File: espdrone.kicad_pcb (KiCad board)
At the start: 6 copper layers, 60 x 60 mm, 504 parts, among them J10 Conn_01x04, J11 Conn_01x04, J12 Conn_01x04, J4 Conn_01x06, J5 Conn_Coaxial, J6 Conn_01x06, J7 Conn_01x06, J8 Conn_01x04, J9 Conn_01x04, Q1 NMOS, Q10 NMOS, Q11 NMOS, Q12 NMOS, Q13 NMOS, Q14 NMOS, Q15 NMOS, Q16 NMOS, Q17 NMOS, Q18 NMOS, Q19 NMOS, Q2 NMOS, Q20 NMOS, Q21 NMOS, Q22 NMOS, Q23 NMOS, Q24 NMOS, Q25 NMOS, Q26 NMOS, Q27 NMOS, Q28 NMOS, Q3 NMOS, Q4 NMOS, Q5 NMOS, Q6 NMOS, Q7 NMOS, Q8 NMOS, Q9 NMOS, U10 FPC-1.0FX-15PWCR-H20, U11 VL53L1CXV0FY1, U12 LIS2MDL, U13 LSM6DS3, U14 PMW3901MB-TXQT_C43496881, U15 STM32G071K8U6, U16 DRV8328ARUYR, U17 INA180A2, U18 STM32G071K8U6, U19 DRV8328ARUYR, U2 USBLC6-2P6, U20 INA180A2, U21 STM32G071K8U6, U22 DRV8328ARUYR, U23 INA180A2, U24 STM32G071K8U6, U25 DRV8328ARUYR, U26 INA180A2, U3 W25Q128JVP, U4 ESP32-C5HF4, U5 LFD182G45DCHD277, U6 TLV62569DBV, U7 XC6206P182MR_C347373, U8 TPS63070RNMR, U9 TPS2121RUXR, Y1 Crystal_GND24, Y2 Crystal_GND24

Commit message: Do local layout of power sheet
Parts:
- moved C59 55.1 mm to (281.2, 112.9)
- moved C61 54.2 mm to (281.2, 114.7)
- moved C65 54.2 mm to (281.2, 116.7)
- moved R38 43.2 mm to (264.2, 87.0), turned to 90 degrees
- moved R29 41.1 mm to (260.2, 91.0)
- moved R37 41.0 mm to (264.2, 89.0), turned to 90 degrees
- moved R30 40.7 mm to (258.2, 91.0)
- moved L3 39.9 mm to (264.5, 96.4), turned to -90 degrees
- moved R31 39.0 mm to (260.0, 98.6)
- moved C74 38.4 mm to (277.6, 97.1), turned to 180 degrees
- moved TP2 37.9 mm to (280.4, 103.8)
- moved TP1 37.9 mm to (275.4, 103.8)
- moved R36 37.6 mm to (261.2, 88.5), turned to 90 degrees
- moved C73 34.3 mm to (257.5, 108.0), turned to -90 degrees
- moved R33 34.0 mm to (260.2, 88.5), turned to 90 degrees
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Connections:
- R31 pad 1: Net-(R31-Pad1) -> FB_DCDC
- R32 pad 2: Net-(R31-Pad1) -> FB_DCDC

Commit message: Get rid of 1.8V LDO and use P4 VDDO4 instead
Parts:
- removed C59, C65: 1u, Capacitor_SMD:C_0402_1005Metric
- removed C61: 100n, Capacitor_SMD:C_0402_1005Metric
- removed U7: XC6206P182MR_C347373, easyeda2kicad:SOT-23-3_L3.0-W1.7-P0.95-LS2.9-BR
- moved C74 5.84 mm to (273.6, 92.9)
- moved TP1 5.84 mm to (271.4, 99.5)
- moved TP2 5.84 mm to (276.4, 99.5)
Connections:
- C33 pad 1: /MCU/VDDO_4 -> VDDO_4
- C88 pad 2: +1V8 -> VDDO_4
- C90 pad 2: +1V8 -> VDDO_4
- C92 pad 2: +1V8 -> VDDO_4
- U1 pad 74: /MCU/VDDO_4 -> VDDO_4
- U14 pad 2: +1V8 -> VDDO_4

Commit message: Do some ESC layouting
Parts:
- removed U17: INA180A2, Package_TO_SOT_SMD:SOT-23-5
- added U27: INA190A3IDCKR, easyeda2kicad:SC-70-6_L2.0-W1.3-P0.65-LS2.1-BL, F.Cu at (197.4, 70.5)
- added U28: INA190A3IDCKR, easyeda2kicad:SC-70-6_L2.0-W1.3-P0.65-LS2.1-BL, F.Cu at (197.4, 76.6)
- added U29: INA190A3IDCKR, easyeda2kicad:SC-70-6_L2.0-W1.3-P0.65-LS2.1-BL, F.Cu at (202.6, 70.5)
- added U7: INA190A3IDCKR, easyeda2kicad:SC-70-6_L2.0-W1.3-P0.65-LS2.1-BL, B.Cu at (127.2, 86.8)
- C102, C103, C105, C107, C109, C110, C111, C117, C119, R62, R63, R65, R66, R71, R72, R77, R80, R85, U16: moved to B.Cu
- TP11, TP12, TP13, TP14, TP15, TP16, TP17, TP18, TP19, TP23, TP24, TP25, TP26, TP27, TP28, TP29, TP30, TP31, TP35, TP36, TP37, TP38, TP39, TP40, TP41, TP42, TP43, TP47, TP48, TP49, TP50, TP51, TP52, TP53, TP54, TP55: footprint TestPoint:TestPoint_Pad_D1.0mm -> easyeda2kicad:TestPoint_Pad_D1.0mm_No_Courtyard
- U20, U23, U26: footprint Package_TO_SOT_SMD:SOT-23-5 -> Package_TO_SOT_SMD:SOT-363_SC-70-6
- moved C73 168.7 mm to (103.2, 176.0)
- moved R34 168.7 mm to (107.2, 174.0)
- moved R35 168.7 mm to (107.2, 176.0)
- moved R39 168.7 mm to (103.2, 174.0)
- moved U9 168.7 mm to (105.2, 175.0)
- moved C60 168.4 mm to (104.8, 161.2)
- moved R29 168.4 mm to (106.8, 160.2)
- moved R30 168.4 mm to (104.8, 160.2)
- moved C64 167.6 mm to (106.8, 156.4)
- moved C70 167.6 mm to (114.1, 154.8)
- moved C71 167.6 mm to (114.1, 152.8)
- moved U8 167.6 mm to (110.2, 157.2)
- moved C62 167.6 mm to (106.0, 152.5)
- moved C63 167.6 mm to (106.0, 154.5)
- moved C68 167.6 mm to (111.1, 159.2)
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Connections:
- Q10 pad 1: Net-(Q10-D) -> /Motors/ESC1/PHASE_C
- Q11 pad 3: Net-(Q11-S) -> /Motors/ESC2/PHASE_A
- Q12 pad 1: Net-(Q11-S) -> /Motors/ESC2/PHASE_A
- Q13 pad 3: Net-(Q13-S) -> /Motors/ESC2/PHASE_B
- Q14 pad 1: Net-(Q13-S) -> /Motors/ESC2/PHASE_B
- Q15 pad 3: Net-(Q15-S) -> /Motors/ESC2/PHASE_C
- Q16 pad 1: Net-(Q15-S) -> /Motors/ESC2/PHASE_C
- Q17 pad 3: Net-(Q17-S) -> /Motors/ESC3/PHASE_A
- Q18 pad 1: Net-(Q17-S) -> /Motors/ESC3/PHASE_A
- Q19 pad 3: Net-(Q19-S) -> /Motors/ESC3/PHASE_B
- Q20 pad 1: Net-(Q19-S) -> /Motors/ESC3/PHASE_B
- Q21 pad 3: Net-(Q21-S) -> /Motors/ESC3/PHASE_C
- Q22 pad 1: Net-(Q21-S) -> /Motors/ESC3/PHASE_C
- Q23 pad 3: Net-(Q23-S) -> /Motors/ESC4/PHASE_A
- Q24 pad 1: Net-(Q23-S) -> /Motors/ESC4/PHASE_A
- Q25 pad 3: Net-(Q25-S) -> /Motors/ESC4/PHASE_B
- Q26 pad 1: Net-(Q25-S) -> /Motors/ESC4/PHASE_B
- Q27 pad 3: Net-(Q27-S) -> /Motors/ESC4/PHASE_C
- Q28 pad 1: Net-(Q27-S) -> /Motors/ESC4/PHASE_C
- Q5 pad 3: Net-(Q5-S) -> /Motors/ESC1/PHASE_A
- Q6 pad 1: Net-(Q5-S) -> /Motors/ESC1/PHASE_A
- Q7 pad 3: Net-(Q7-S) -> /Motors/ESC1/PHASE_B
- Q8 pad 1: Net-(Q7-S) -> /Motors/ESC1/PHASE_B
- Q9 pad 3: Net-(Q10-D) -> /Motors/ESC1/PHASE_C
- R122 pad 2: Net-(R122-Pad2) -> Net-(U28-OUT)
- R147 pad 2: Net-(R147-Pad2) -> Net-(U29-OUT)
- R97 pad 2: Net-(R97-Pad2) -> Net-(U27-OUT)

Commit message: Progress on bridge layout
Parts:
- C109, C110, C111, R77, R80, R85: moved to F.Cu
- R69, R70, R73, R74, R81, R82: moved to B.Cu
- moved Q10 18.0 mm to (129.5, 61.9)
- moved Q9 18.0 mm to (129.8, 65.8)
- moved TP22 18.0 mm to (126.5, 58.6)
- moved Q7 17.6 mm to (124.8, 65.8)
- moved Q8 17.6 mm to (124.4, 61.9)
- moved TP21 17.6 mm to (127.8, 58.5)
- moved R71 17.5 mm to (124.8, 65.8)
- moved C117 17.5 mm to (127.1, 70.2)
- moved C119 17.5 mm to (127.6, 68.7)
- moved R72 17.5 mm to (126.6, 68.7)
- moved U7 17.5 mm to (125.1, 69.4)
- moved Q5 17.3 mm to (119.8, 65.8)
- moved TP20 17.3 mm to (122.9, 58.5)
- moved Q6 17.3 mm to (119.5, 61.9)
- moved C110 16.8 mm to (125.5, 70.0), turned to 180 degrees
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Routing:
- net /Motors/ESC1/LSS: track 0.00 -> 17.9 mm, vias 0 -> 3
- net /Motors/ESC1/PHASE_C: track 0.00 -> 15.4 mm
- net /Motors/ESC1/PHASE_B: track 0.00 -> 14.9 mm
- net /Motors/ESC1/PHASE_A: track 0.00 -> 14.8 mm
- net Net-(Q10-G): track 0.00 -> 11.7 mm, vias 0 -> 1
- net GND: track 0.00 -> 11.6 mm
- net Net-(Q9-G): track 0.00 -> 9.36 mm, vias 0 -> 1
- net /Motors/ESC1/ISENSE: track 0.00 -> 1.01 mm
- net Net-(U7-OUT): track 0.00 -> 0.92 mm
- net +BATT: track 0.00 -> 0.11 mm, vias 0 -> 36

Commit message: Okayish bridge layout
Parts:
- moved R85 8.26 mm to (123.2, 75.2), turned to -90 degrees
- moved R82 6.14 mm to (126.1, 73.5), turned to 180 degrees
- moved R80 5.66 mm to (122.0, 75.2), turned to -90 degrees
- moved C111 5.10 mm to (125.7, 72.4)
- moved C110 4.15 mm to (122.2, 72.4)
- moved R81 4.01 mm to (126.1, 72.0), turned to 180 degrees
- moved R77 3.81 mm to (120.8, 75.2), turned to -90 degrees
- moved C109 3.32 mm to (118.5, 72.4)
- moved C105 2.14 mm to (116.5, 77.8), turned to -90 degrees
- moved C107 1.63 mm to (118.4, 78.3)
- moved TP22 0.78 mm to (127.2, 58.6)
- moved Q5 0.36 mm to (119.4, 65.8)
- moved Q6 0.36 mm to (119.1, 61.9)
- moved TP20 0.36 mm to (122.6, 58.5)
- moved Q10 0.28 mm to (129.8, 61.9)
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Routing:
- net /Motors/ESC1/GLA: track 0.00 -> 12.5 mm
- net /Motors/ESC1/GHA: track 0.00 -> 7.53 mm
- net Net-(Q7-G): track 0.32 -> 7.20 mm, vias 0 -> 1
- net Net-(Q8-G): track 0.00 -> 6.35 mm, vias 0 -> 1
- net GND: track 11.6 -> 17.9 mm, vias 0 -> 12
- net Net-(Q10-G): track 11.7 -> 17.8 mm
- net Net-(U16-VDSLVL): track 0.00 -> 5.92 mm
- net /Motors/ESC1/GHB: track 0.00 -> 5.52 mm
- net /Motors/ESC1/BSTA: track 0.00 -> 5.22 mm, vias 0 -> 1
- net /Motors/ESC1/GLB: track 0.00 -> 5.11 mm
- net +BATT: track 0.11 -> 5.09 mm
- net Net-(U16-DT): track 0.00 -> 4.37 mm
- net /Motors/ESC1/GHC: track 0.00 -> 4.19 mm
- net Net-(Q9-G): track 9.36 -> 13.5 mm
- net Net-(U16-BSTC): track 0.00 -> 3.69 mm, vias 0 -> 1
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- added copper zone on F.Cu, net */LSS
- added copper zone on B.Cu, net /Motors/ESC1/LSS
- added copper zone on F.Cu, net /Motors/ESC1/LSS
- added copper zone on F.Cu, net /Motors/ESC1/PHASE_A

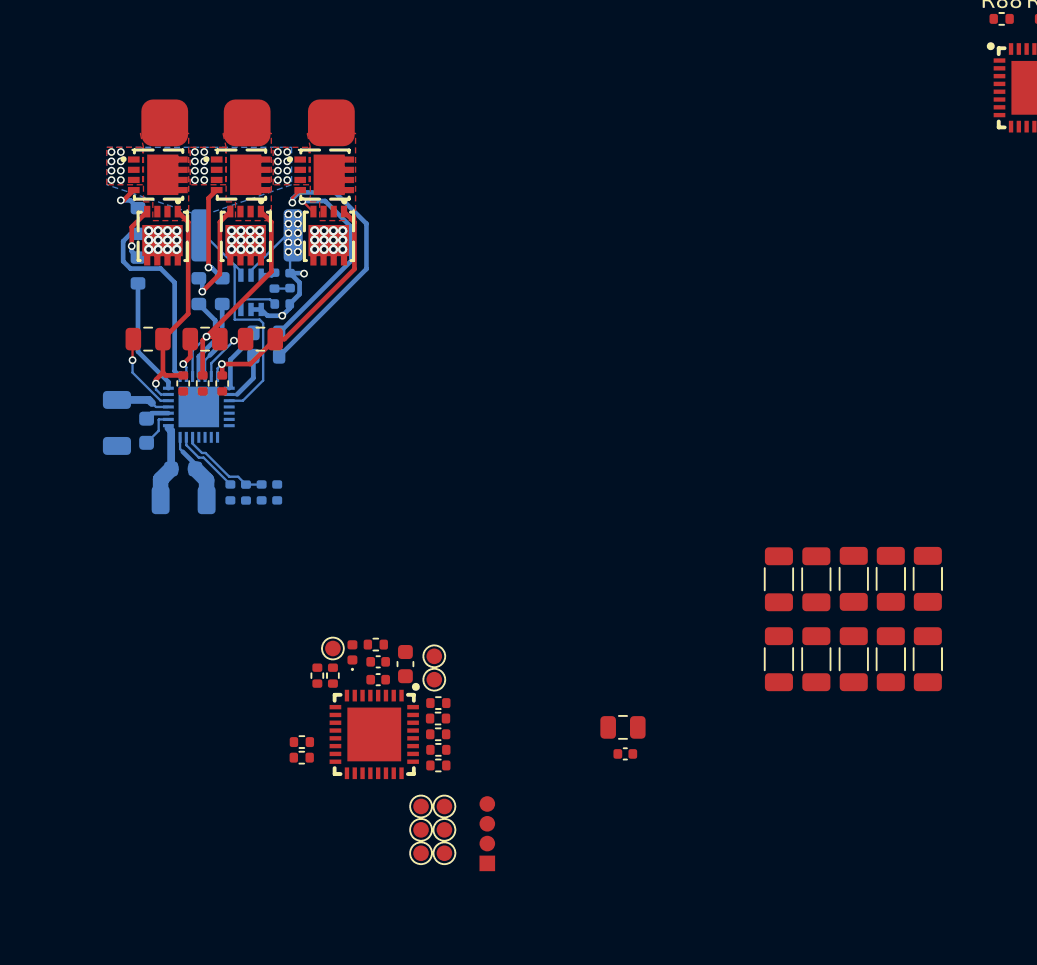
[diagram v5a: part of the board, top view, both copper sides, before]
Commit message: ESC mostly done apart from STM routing
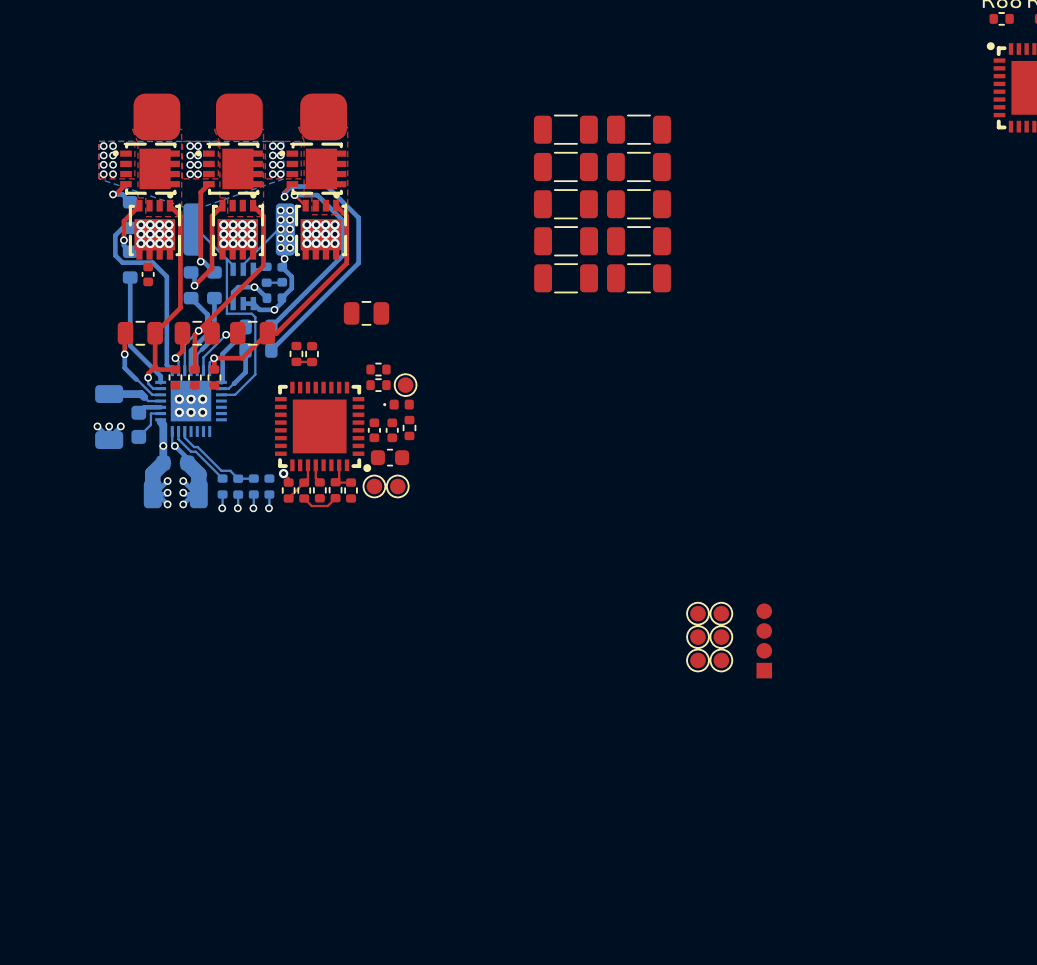
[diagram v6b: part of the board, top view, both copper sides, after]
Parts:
- moved C112 43.4 mm to (118.5, 68.2), turned to 90 degrees
- moved C122 37.0 mm to (145.3, 59.0), turned to 180 degrees
- moved C118 35.1 mm to (150.0, 59.0), turned to 0 degrees
- moved C125 33.6 mm to (145.3, 61.4), turned to 180 degrees
- moved C120 33.6 mm to (150.0, 61.4), turned to 0 degrees
- moved C121 32.3 mm to (150.0, 63.8), turned to 0 degrees
- moved C114 31.3 mm to (150.0, 66.1), turned to 0 degrees
- moved C115 31.2 mm to (132.5, 70.8), turned to 180 degrees
- moved C113 30.7 mm to (150.0, 68.5), turned to 0 degrees
- moved C124 30.3 mm to (145.3, 63.8), turned to 180 degrees
- moved C123 27.0 mm to (145.3, 66.1), turned to 180 degrees
- moved R68 25.9 mm to (128.0, 73.3), turned to -90 degrees
- moved R67 24.9 mm to (129.0, 73.4), turned to 90 degrees
- moved C116 23.6 mm to (145.3, 68.5), turned to 180 degrees
- moved J8 21.6 mm to (155.8, 91.7)
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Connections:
- U15 pad 10: unconnected-(U15-PA3-Pad10) -> /Motors/ESC1/VSENSE_REF
- U15 pad 8: /Motors/ESC1/VSENSE_REF -> unconnected-(U15-PA1-Pad8)
- U18 pad 10: unconnected-(U18-PA3-Pad10) -> /Motors/ESC2/VSENSE_REF
- U18 pad 8: /Motors/ESC2/VSENSE_REF -> unconnected-(U18-PA1-Pad8)
- U21 pad 10: unconnected-(U21-PA3-Pad10) -> /Motors/ESC3/VSENSE_REF
- U21 pad 8: /Motors/ESC3/VSENSE_REF -> unconnected-(U21-PA1-Pad8)
- U24 pad 10: unconnected-(U24-PA3-Pad10) -> /Motors/ESC4/VSENSE_REF
- U24 pad 8: /Motors/ESC4/VSENSE_REF -> unconnected-(U24-PA1-Pad8)
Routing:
- net GND: track 17.9 -> 26.9 mm, vias 12 -> 28
- net +BATT: track 5.09 -> 8.60 mm, vias 36 -> 40
- net +3V3: track 2.80 -> 5.53 mm, vias 0 -> 3
- net /Motors/ESC1/VSENSE_B: track 0.00 -> 2.64 mm
- net /Motors/ESC1/VSENSE_REF: track 0.00 -> 2.42 mm
- net /Motors/ESC1/VSENSE_A: track 0.00 -> 2.18 mm
- net Net-(U15-PB4): track 0.00 -> 1.21 mm
- net /Motors/ESC1/VSENSE: track 0.00 -> 1.00 mm
- added copper zone on F.Cu, net /Motors/ESC1/PHASE_B
- added copper zone on F.Cu, net /Motors/ESC1/PHASE_C
- removed copper zone on F.Cu, net */LSS

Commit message: Begin routing STM
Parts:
- moved R84 9.02 mm to (131.8, 83.2), turned to 90 degrees
- moved R83 8.28 mm to (130.8, 83.2), turned to -90 degrees
- moved R75 3.94 mm to (126.8, 83.2)
- moved R76 3.93 mm to (127.8, 83.2)
- moved R64 3.84 mm to (133.2, 81.2), turned to 0 degrees
- moved R79 2.51 mm to (129.8, 83.2), turned to 90 degrees
- moved R78 1.16 mm to (128.8, 83.2)
- moved C102 0.79 mm to (119.5, 82.5)
- moved C103 0.79 mm to (119.5, 80.5)
- moved R62 0.78 mm to (125.5, 81.8)
- moved R63 0.78 mm to (122.5, 81.8)
- moved R66 0.78 mm to (124.5, 81.8)
- moved R65 0.78 mm to (123.5, 81.9)
- moved R68 0.75 mm to (128.8, 73.5)
- moved R67 0.75 mm to (129.8, 73.5)
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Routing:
- net /Motors/ESC1/VSENSE_C: track 0.00 -> 13.3 mm
- net GND: track 26.9 -> 15.3 mm, vias 28 -> 23
- net /Motors/ESC1/NFAULT: track 0.00 -> 11.2 mm, vias 0 -> 1
- net /Motors/ESC1/NSLEEP: track 0.00 -> 9.52 mm, vias 0 -> 1
- net /Motors/ESC1/B_LOW: track 0.00 -> 9.47 mm, vias 0 -> 1
- net /Motors/ESC1/A_LOW: track 0.00 -> 8.89 mm, vias 0 -> 1
- net /Motors/ESC1/C_LOW: track 0.00 -> 8.67 mm, vias 0 -> 1
- net /Motors/ESC1/ISENSE: track 1.01 -> 9.25 mm, vias 0 -> 2
- net /Motors/ESC1/VSENSE_A: track 2.18 -> 9.57 mm
- net +BATT: track 8.60 -> 1.47 mm, vias 40 -> 36
- net /Motors/ESC1/VSENSE_B: track 2.64 -> 8.55 mm
- net /Motors/ESC1/VSENSE_REF: track 2.42 -> 7.09 mm, vias 0 -> 2
- net /Motors/ESC1/A_HIGH: track 0.00 -> 4.26 mm, vias 0 -> 1
- net /Motors/ESC1/B_HIGH: track 0.00 -> 4.04 mm, vias 0 -> 1
- net /Motors/ESC1/C_HIGH: track 0.00 -> 3.97 mm, vias 0 -> 1
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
